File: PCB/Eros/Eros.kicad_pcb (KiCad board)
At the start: 4 copper layers, 65 x 71 mm, 114 parts, among them IC1 ADS1292RIPBS, J1 USB_C_PowerOnly_6P, J2 UART, J3 Li-ion, J4 Conn_01x08_Socket, J5 AudioJack3, J6 Micro_SD_Card, J7 Conn_01x03_Socket, Q1 BC817, SW1 SW_Push, SW2 SW_Push, SW4 SW_Push, SW5 SW_Push, SW6 SW_SPDT, U1 ESP32-WROOM-32E, U2 LIS3DH, U3 MCP73831-2-OT, U4 AP2112K-3.3, U6 MCP100-315D

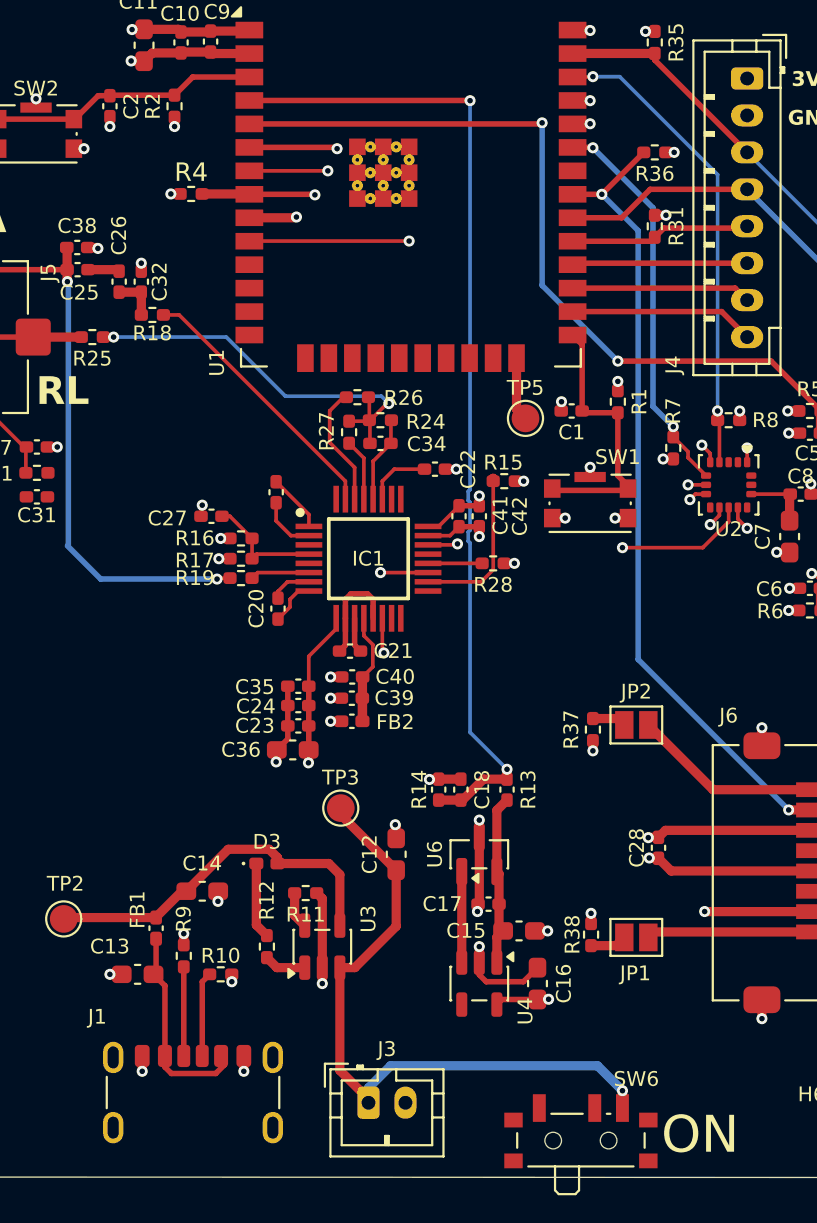
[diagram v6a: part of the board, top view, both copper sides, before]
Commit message: wire HSPI
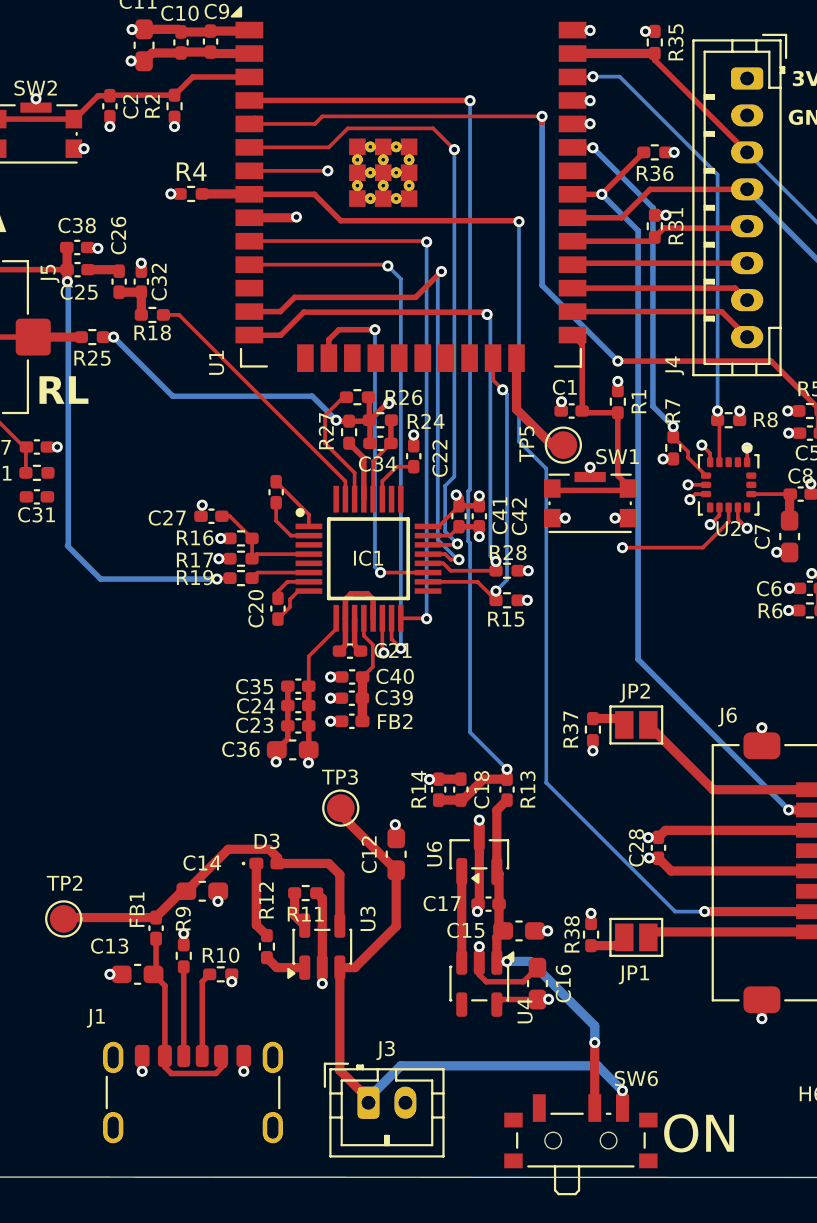
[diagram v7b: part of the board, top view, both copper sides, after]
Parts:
- moved R15 6.45 mm to (191.5, 89.2)
- moved TP5 2.51 mm to (194.6, 80.8)
- moved C22 1.35 mm to (186.4, 81.5), turned to 90 degrees
- moved R28 0.85 mm to (191.5, 87.7)
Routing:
- net MICRO_SD_CS: track 11.8 -> 65.9 mm
- net PWDN: track 0.00 -> 30.4 mm, vias 0 -> 2
- net HSPI_MISO: track 0.00 -> 29.3 mm, vias 0 -> 2
- net DRDY: track 6.39 -> 35.6 mm
- net HSPI_SCK: track 2.93 -> 31.4 mm, vias 0 -> 2
- net START: track 8.65 -> 31.4 mm, vias 1 -> 2
- net HSPI_MOSI: track 2.57 -> 19.6 mm, vias 1 -> 2
- net Net-(SW6-B): track 9.30 -> 20.5 mm, vias 0 -> 2
- net HSPI_CS: track 8.76 -> 17.8 mm, vias 0 -> 2
- net Net-(U1-IO2): track 3.46 -> 6.11 mm
- net Net-(C34-Pad1): track 22.0 -> 20.3 mm, vias 2 -> 3
- net BUTTON_2: track 51.4 -> 52.7 mm
- net GND: track 75.9 -> 76.5 mm, vias 47 -> 48
- net VCAP2: track 3.53 -> 3.00 mm

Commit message: wire everything
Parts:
- moved D6 53.9 mm to (177.5, 89.2)
- moved R23 47.7 mm to (173.9, 88.3)
- moved R22 47.6 mm to (173.9, 87.2)
- moved C33 47.5 mm to (171.4, 93.2), turned to 0 degrees
- moved C30 45.2 mm to (173.9, 89.5), turned to 180 degrees
- moved C29 44.5 mm to (171.5, 90.7), turned to 180 degrees
- moved R20 42.5 mm to (171.5, 92.1)
- moved D1 35.3 mm to (175.2, 92.2), turned to 90 degrees
- moved D4 34.7 mm to (166.0, 84.1), turned to 90 degrees
- moved D5 30.4 mm to (169.4, 83.2), turned to 90 degrees
- moved C25 8.65 mm to (172.5, 78.9)
- moved C26 8.65 mm to (174.7, 79.5)
- moved C32 8.65 mm to (175.9, 79.5)
- moved C38 8.65 mm to (172.4, 77.7)
- moved R18 8.65 mm to (176.5, 81.3)
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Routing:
- net BUZZER: track 0.00 -> 68.6 mm, vias 0 -> 2
- net AVDD: track 7.76 -> 67.9 mm, vias 1 -> 4
- net IN2N: track 0.00 -> 22.8 mm, vias 0 -> 2
- net IN3N: track 0.00 -> 19.2 mm, vias 0 -> 2
- net ADC: track 53.8 -> 71.8 mm
- net RA: track 18.0 -> 30.5 mm
- net IN1N: track 0.00 -> 11.3 mm, vias 0 -> 2
- net IN1P: track 6.54 -> 14.7 mm
- net IN3P: track 14.6 -> 7.21 mm
- net GND: track 76.5 -> 83.8 mm, vias 48 -> 56
- net LA: track 51.6 -> 44.4 mm
- net IN2P: track 3.20 -> 7.71 mm
- net Net-(IC1-PGA2N): track 2.26 -> 5.62 mm
- net Net-(C29-Pad2): track 0.00 -> 2.54 mm
- net Net-(C29-Pad1): track 0.00 -> 2.47 mm
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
